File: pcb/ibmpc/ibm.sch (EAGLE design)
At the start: 32 parts, among them J2 ATX24RH

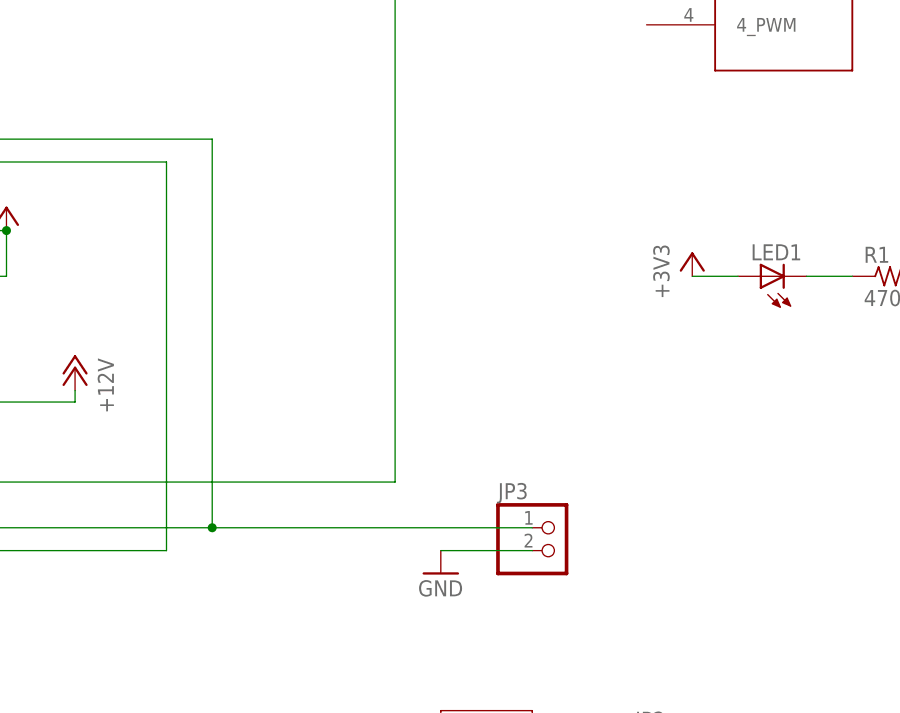
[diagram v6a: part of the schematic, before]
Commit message: LED now shows power good signal
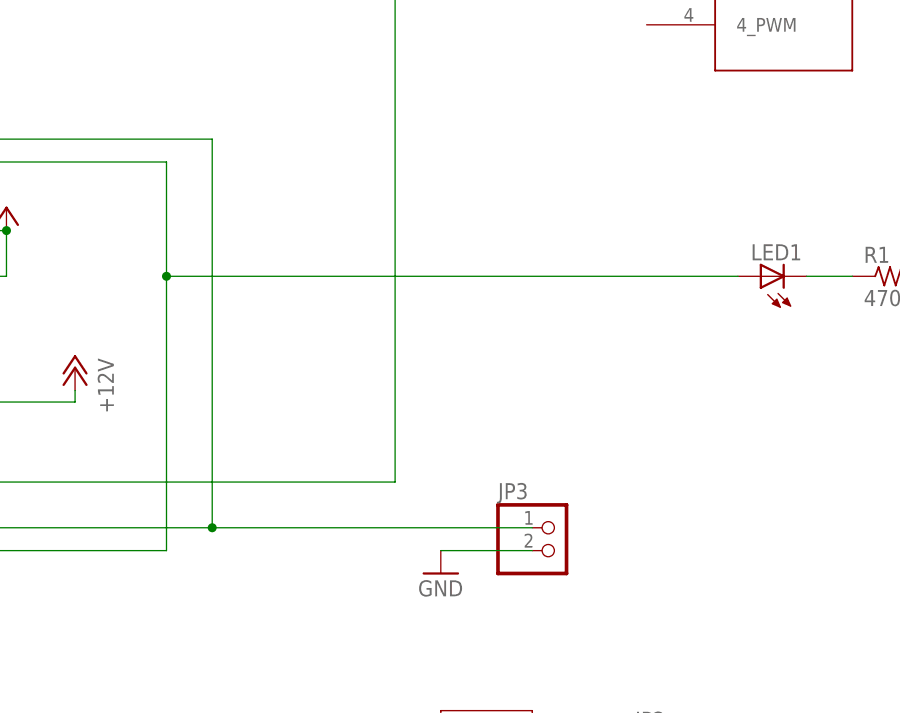
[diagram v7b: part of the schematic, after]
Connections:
- net +3V3: no longer LED1.A
- net N$4: now also LED1.A
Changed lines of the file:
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@@
 <part name="GND10" library="supply1" library_urn="urn:adsk.eagle:library:371" deviceset="GND" device=""/>
 <part name="LED1" library="adafruit" deviceset="LED" device="5MM"/>
-<part name="+3V4" library="supply1" library_urn="urn:adsk.eagle:library:371" deviceset="+3V3" device=""/>
 <part name="R1" library="adafruit" deviceset="R-US_" device="0207/10" value="470"/>
 <part name="GND12" library="supply1" library_urn="urn:adsk.eagle:library:371" deviceset="GND" device=""/>
@@
 <attribute name="NAME" x="261.112" y="194.056" size="1.778" layer="95" rot="R180"/>
 <attribute name="VALUE" x="261.112" y="196.215" size="1.778" layer="96" rot="R180"/>
-</instance>
-<instance part="+3V4" gate="G$1" x="248.92" y="193.04" smashed="yes">
-<attribute name="VALUE" x="246.38" y="187.96" size="1.778" layer="96" rot="R90"/>
 </instance>
 <instance part="R1" gate="G$1" x="271.78" y="190.5" smashed="yes">
@@
 <wire x1="114.3" y1="254" x2="132.08" y2="254" width="0.1524" layer="91"/>
 </segment>
-<segment>
-<pinref part="+3V4" gate="G$1" pin="+3V3"/>
-<pinref part="LED1" gate="G$1" pin="A"/>
-<wire x1="248.92" y1="190.5" x2="254" y2="190.5" width="0.1524" layer="91"/>
-</segment>
 </net>
 <net name="N$2" class="0">
@@
 <pinref part="J2" gate="G$1" pin="PWR_OK"/>
 <wire x1="109.22" y1="160.02" x2="190.5" y2="160.02" width="0.1524" layer="91"/>
-<wire x1="190.5" y1="160.02" x2="190.5" y2="203.2" width="0.1524" layer="91"/>
+<wire x1="190.5" y1="160.02" x2="190.5" y2="190.5" width="0.1524" layer="91"/>
+<wire x1="190.5" y1="190.5" x2="190.5" y2="203.2" width="0.1524" layer="91"/>
 <wire x1="190.5" y1="203.2" x2="63.5" y2="203.2" width="0.1524" layer="91"/>
 <wire x1="63.5" y1="203.2" x2="63.5" y2="228.6" width="0.1524" layer="91"/>
 <pinref part="U$1" gate="G$1" pin="PWR_OK"/>
 <wire x1="63.5" y1="228.6" x2="78.74" y2="228.6" width="0.1524" layer="91"/>
-</segment>
-</net>
+<pinref part="LED1" gate="G$1" pin="A"/>
+<wire x1="190.5" y1="190.5" x2="254" y2="190.5" width="0.1524" layer="91"/>
+<junction x="190.5" y="190.5"/>
+</segment>
+</net>

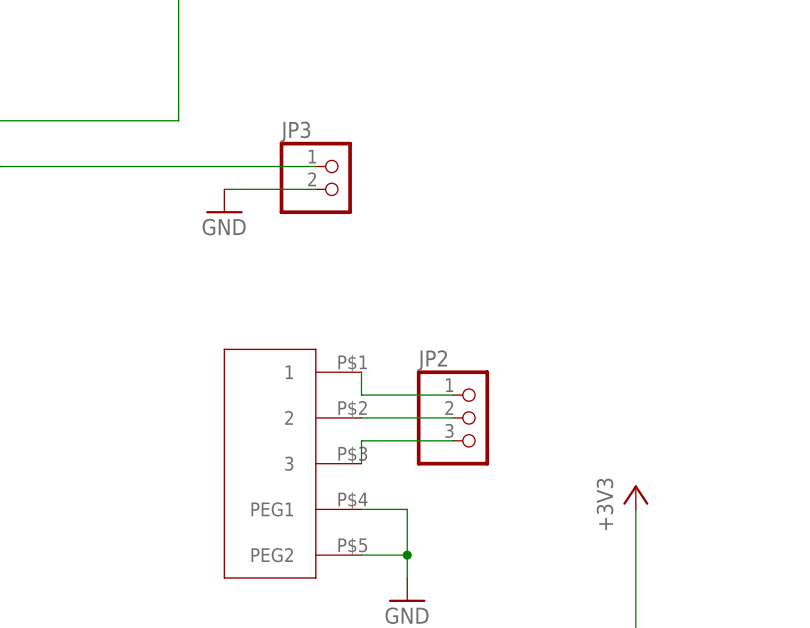
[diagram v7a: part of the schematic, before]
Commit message: connected up switch, adjusted mounting hole
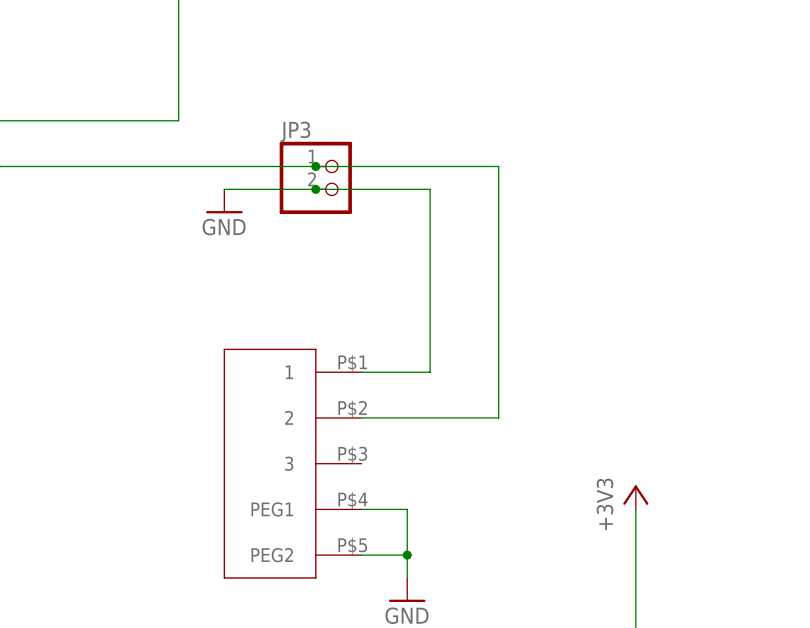
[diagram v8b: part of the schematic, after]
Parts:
- removed JP2: (no value), pinhead:PINHD-1X3
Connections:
- removed net N$10: JP2.2, U$4.2
- removed net N$11: JP2.3, U$4.3
- removed net N$9: JP2.1, U$4.1
- net GND: now also U$4.1
- net N$3: now also U$4.2
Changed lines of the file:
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@@
 <part name="U$4" library="apricot" deviceset="ROCKSW" device=""/>
 <part name="GND4" library="supply1" library_urn="urn:adsk.eagle:library:371" deviceset="GND" device=""/>
-<part name="JP2" library="pinhead" library_urn="urn:adsk.eagle:library:325" deviceset="PINHD-1X3" device="" package3d_urn="urn:adsk.eagle:package:22458/2"/>
 <part name="JP3" library="pinhead" library_urn="urn:adsk.eagle:library:325" deviceset="PINHD-1X2" device="" package3d_urn="urn:adsk.eagle:package:22435/2"/>
 <part name="GND10" library="supply1" library_urn="urn:adsk.eagle:library:371" deviceset="GND" device=""/>
@@
 <instance part="GND4" gate="1" x="241.3" y="114.3" smashed="yes">
 <attribute name="VALUE" x="238.76" y="111.76" size="1.778" layer="96"/>
-</instance>
-<instance part="JP2" gate="A" x="248.92" y="134.62" smashed="yes">
-<attribute name="NAME" x="242.57" y="140.335" size="1.778" layer="95"/>
-<attribute name="VALUE" x="242.57" y="127" size="1.778" layer="96"/>
 </instance>
 <instance part="JP3" gate="G$1" x="233.68" y="160.02" smashed="yes">
@@
 <pinref part="JP3" gate="G$1" pin="2"/>
 <wire x1="220.98" y1="160.02" x2="231.14" y2="160.02" width="0.1524" layer="91"/>
+<wire x1="231.14" y1="160.02" x2="243.84" y2="160.02" width="0.1524" layer="91"/>
+<wire x1="243.84" y1="160.02" x2="243.84" y2="139.7" width="0.1524" layer="91"/>
+<junction x="231.14" y="160.02"/>
+<pinref part="U$4" gate="G$1" pin="1"/>
+<wire x1="243.84" y1="139.7" x2="236.22" y2="139.7" width="0.1524" layer="91"/>
 </segment>
 <segment>
@@
 <wire x1="195.58" y1="162.56" x2="231.14" y2="162.56" width="0.1524" layer="91"/>
 <junction x="195.58" y="162.56"/>
+<wire x1="231.14" y1="162.56" x2="251.46" y2="162.56" width="0.1524" layer="91"/>
+<wire x1="251.46" y1="162.56" x2="251.46" y2="134.62" width="0.1524" layer="91"/>
+<junction x="231.14" y="162.56"/>
+<pinref part="U$4" gate="G$1" pin="2"/>
+<wire x1="251.46" y1="134.62" x2="236.22" y2="134.62" width="0.1524" layer="91"/>
 </segment>
 </net>
@@
 </segment>
 </net>
-<net name="N$9" class="0">
-<segment>
-<pinref part="U$4" gate="G$1" pin="1"/>
-<pinref part="JP2" gate="A" pin="1"/>
-<wire x1="236.22" y1="139.7" x2="236.22" y2="137.16" width="0.1524" layer="91"/>
-<wire x1="236.22" y1="137.16" x2="246.38" y2="137.16" width="0.1524" layer="91"/>
-</segment>
-</net>
-<net name="N$10" class="0">
-<segment>
-<pinref part="U$4" gate="G$1" pin="2"/>
-<pinref part="JP2" gate="A" pin="2"/>
-<wire x1="236.22" y1="134.62" x2="246.38" y2="134.62" width="0.1524" layer="91"/>
-</segment>
-</net>
-<net name="N$11" class="0">
-<segment>
-<pinref part="U$4" gate="G$1" pin="3"/>
-<pinref part="JP2" gate="A" pin="3"/>
-<wire x1="236.22" y1="129.54" x2="236.22" y2="132.08" width="0.1524" layer="91"/>
-<wire x1="236.22" y1="132.08" x2="246.38" y2="132.08" width="0.1524" layer="91"/>
-</segment>
-</net>
